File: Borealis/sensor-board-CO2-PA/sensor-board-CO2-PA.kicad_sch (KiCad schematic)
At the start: 3 parts, among them J2 Conn_01x03_Pin (data connecti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, J5 Conn_01x03_Pin (power connect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

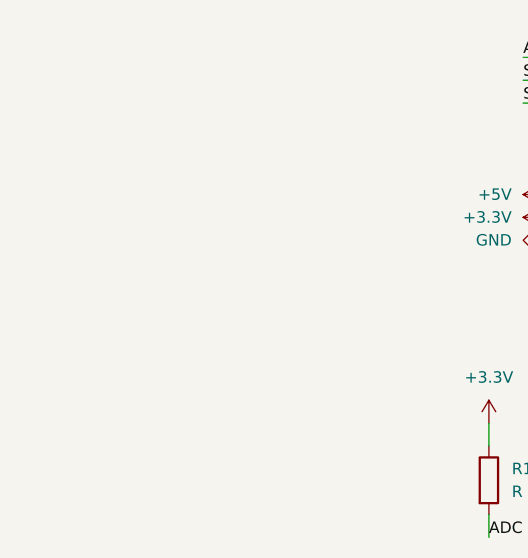
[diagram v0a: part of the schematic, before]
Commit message: Added mainboard and temerature board
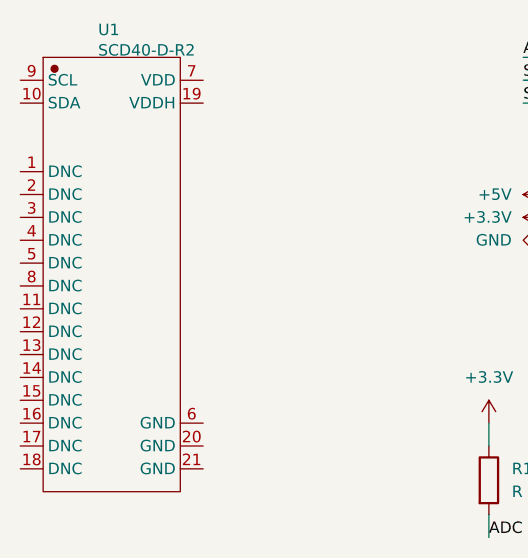
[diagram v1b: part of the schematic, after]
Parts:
- added U1: SCD40-D-R2, batteryholder:SCD40 footprint, symbol teset-altium-import:root_0_SCD40-D-R2_
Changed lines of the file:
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@@
+	)
+	(symbol
+		(lib_id "teset-altium-import:root_0_SCD40-D-R2_")
+		(at 100.33 85.09 0)
+		(unit 1)
+		(exclude_from_sim no)
+		(in_bom yes)
+		(on_board yes)
+		(dnp no)
+		(property "Reference" "U1"
+			(at 98.814 58.643 0)
+			(effects
+				(font
+					(size 1.27 1.27)
+				)
+				(justify left bottom)
+			)
+		)
+		(property "Value" "SCD40-D-R2"
+			(at 98.814 60.916 0)
+			(effects
+				(font
+					(size 1.27 1.27)
+				)
+				(justify left bottom)
+			)
+		)
+		(property "Footprint" "batteryholder:SCD40 footprint"
+			(at 100.33 85.09 0)
+			(effects
+				(font
+					(size 1.27 1.27)
+				)
+				(hide yes)
+			)
+		)
+		(property "Datasheet" ""
+			(at 100.33 85.09 0)
+			(effects
+				(font
+					(size 1.27 1.27)
+				)
+				(hide yes)
+			)
+		)
+		(property "Description" ""
+			(at 100.33 85.09 0)
+			(effects
+				(font
+					(size 1.27 1.27)
+				)
+				(hide yes)
+			)
+		)
+		(property "CONTRIBUTOR" "LCSC"
+			(at 100.33 85.09 0)
+			(effects
+				(font
+					(size 1.27 1.27)
+				)
+				(justify left bottom)
+				(hide yes)
+			)
+		)
+		(property "SUPPLIER" "LCSC"
+			(at 100.33 85.09 0)
+			(effects
+				(font
+					(size 1.27 1.27)
+				)
+				(justify left bottom)
+				(hide yes)
+			)
+		)
+		(property "SUPPLIER PART" "C9900009940"
+			(at 100.33 85.09 0)
+			(effects
+				(font
+					(size 1.27 1.27)
+				)
+				(justify left bottom)
+				(hide yes)
+			)
+		)
+		(property "MANUFACTURER" "null"
+			(at 100.33 85.09 0)
+			(effects
+				(font
+					(size 1.27 1.27)
+				)
+				(justify left bottom)
+				(hide yes)
+			)
+		)
+		(property "MANUFACTURER PART" "SCD40-D-R2"
+			(at 100.33 85.09 0)
+			(effects
+				(font
+					(size 1.27 1.27)
+				)
+				(justify left bottom)
+				(hide yes)
+			)
+		)
+		(property "JLCPCB PART CLASS" "Extended Part"
+			(at 100.33 85.09 0)
+			(effects
+				(font
+					(size 1.27 1.27)
+				)
+				(justify left bottom)
+				(hide yes)
+			)
+		)
+		(property "SPICEPRE" "U"
+			(at 100.33 85.09 0)
+			(effects
+				(font
+					(size 1.27 1.27)
+				)
+				(justify left bottom)
+				(hide yes)
+			)
+		)
+		(property "SPICESYMBOLNAME" "SCD40-D-R2"
+			(at 100.33 85.09 0)
+			(effects
+				(font
+					(size 1.27 1.27)
+				)
+				(justify left bottom)
+				(hide yes)
+			)
+		)
+		(pin "20"
+		)
+		(pin "16"
+		)
+		(pin "19"
+		)
+		(pin "18"
+		)
+		(pin "17"
+		)
+		(pin "12"
+		)
+		(pin "21"
+		)
+		(pin "7"
+		)
+		(pin "13"
+		)
+		(pin "6"
+		)
+		(pin "15"
+		)
+		(pin "14"
+		)
+		(pin "8"
+		)
+		(pin "11"
+		)
+		(pin "5"
+		)
+		(pin "4"
+		)
+		(pin "9"
+		)
+		(pin "10"
+		)
+		(pin "1"
+		)
+		(pin "2"
+		)
+		(pin "3"
+		)
+		(instances
+			(project "sensor-board-CO2-PA"
+				(path "/4dc67bc0-6b27-441a-860a-e697f5d15d5c"
+					(reference "U1")
+					(unit 1)
+				)
+			)
+		)
 	)
 	(symbol

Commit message: Fixed a few things
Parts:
- removed J2: Conn_01x03_Pin (data connection to main board), symbol Connector:Conn_01x03_Pin
- removed J5: Conn_01x03_Pin (power connection to main board), symbol Connector:Conn_01x03_Pin
- added C5: 10microf, BOREALIS:CAPC17595_95N_KEM, symbol 2026-01-23_05-30-51:C0603C104K5RACTU
- added J4, J7: 878-22-004-10-011101, BOREALIS:8782200410011101, symbol 878-22-004-10-011101:878-22-004-10-011101
- added R2: 10K, OptoDevice:R_LDR_4.9x4.2mm_P2.54mm_Vertical, symbol Device:R
- added R3: 10k, OptoDevice:R_LDR_4.9x4.2mm_P2.54mm_Vertical, symbol Device:R
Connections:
- net +3.3V: now also U1.19 (VDDH), U1.7 (VDD), C5.1, J4.2, R2.1, R3.1
- net +5V: now also J4.3
- net ADC: now also J7.3; no longer R1.2
- net GND: now also U1.20 (GND), U1.21 (GND), U1.6 (GND), C5.2, J4.1
- net SCL: now also U1.9 (SCL), J7.1, R3.2
- net SDA: now also U1.10 (SDA), J7.2, R2.2
- new net ID: J4.4, R1.2
- no-connect marks 0 -> 15
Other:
- moved on the sheet: R1, U1

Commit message: Worked on boards
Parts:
- removed J4, J7: 878-22-004-10-011101, BOREALIS:8782200410011101, symbol 878-22-004-10-011101:878-22-004-10-011101
- added H1: MountingHole, MountingHole:MountingHole_2.7mm_M2.5_Pad, symbol Mechanical:MountingHole
- added U2, U3: MAGNETIC POGO CONN., batteryholder:MAGNETIC POGO CONN., symbol magnetic_pogo_conn.:MAGNETIC_POGO_CONN.
- C5: footprint BOREALIS:CAPC17595_95N_KEM -> Capacitor_SMD:C_0805_2012Metric
- R1: renamed from R2; footprint OptoDevice:R_LDR_4.9x4.2mm_P2.54mm_Vertical -> Resistor_SMD:R_0805_2012Metric
- R2: renamed from R3; footprint OptoDevice:R_LDR_4.9x4.2mm_P2.54mm_Vertical -> Resistor_SMD:R_0805_2012Metric
- R3: renamed from R1; footprint OptoDevice:R_LDR_4.9x4.2mm_P2.54mm_Vertical -> Resistor_SMD:R_0805_2012Metric
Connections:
- net +3.3V: now also C5.2, U3.2; no longer C5.1
- net +5V: now also U3.3
- net ADC: now also U2.2
- net GND: now also C5.1, U3.1; no longer C5.2
- net ID: now also U3.4
- net SCL: now also U2.4
- net SDA: now also U2.3
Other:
- moved on the sheet: C5
